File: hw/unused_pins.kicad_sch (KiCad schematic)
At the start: 0 parts

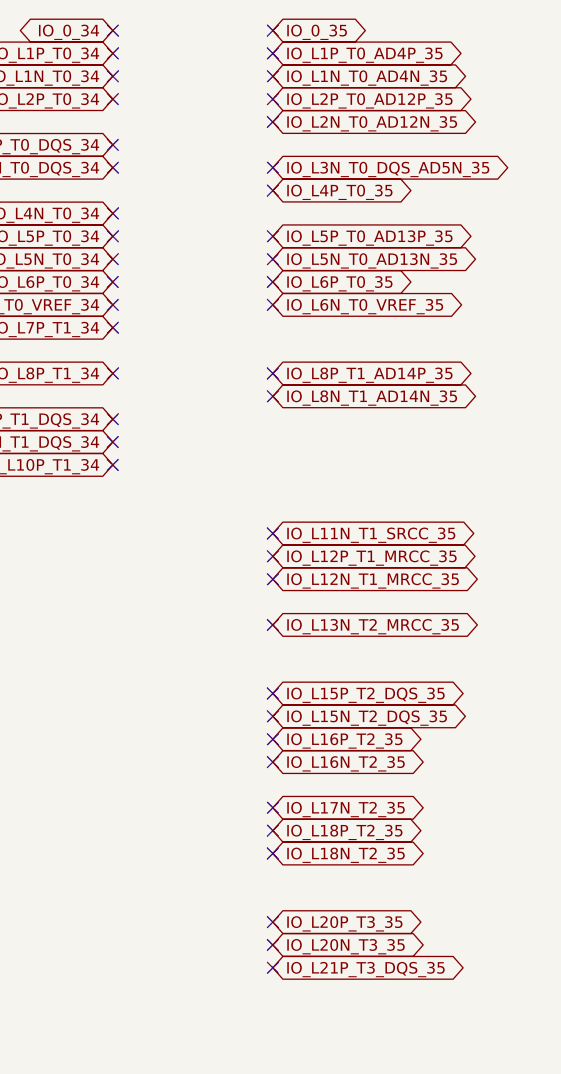
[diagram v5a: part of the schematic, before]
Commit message: finished routing; DRC passes (except for 1 hole violation at push-button)
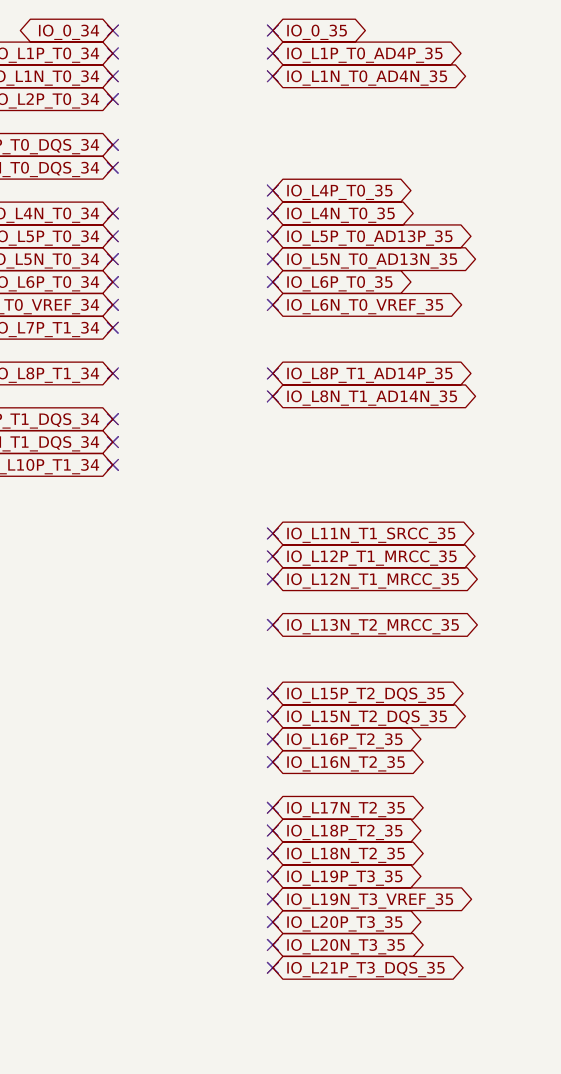
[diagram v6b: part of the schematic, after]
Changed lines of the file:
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@@
   (no_connect (at 69.85 106.68))
   (no_connect (at 69.85 149.86))
-  (no_connect (at 223.52 45.72))
   (no_connect (at 223.52 134.62))
   (no_connect (at 223.52 91.44))
   (no_connect (at 69.85 48.26))
   (no_connect (at 57.15 38.1))
-  (no_connect (at 223.52 40.64))
   (no_connect (at 57.15 93.98))
   (no_connect (at 69.85 129.54))
@@
   (no_connect (at 223.52 106.68))
   (no_connect (at 69.85 137.16))
+  (no_connect (at 223.52 124.46))
   (no_connect (at 57.15 63.5))
   (no_connect (at 223.52 33.02))
@@
   (no_connect (at 223.52 53.34))
   (no_connect (at 57.15 149.86))
+  (no_connect (at 223.52 127))
   (no_connect (at 223.52 48.26))
   (no_connect (at 205.74 38.1))
@@
   (no_connect (at 69.85 83.82))
   (no_connect (at 223.52 68.58))
-  (no_connect (at 223.52 38.1))
+  (no_connect (at 223.52 50.8))
   (no_connect (at 69.85 144.78))
   (no_connect (at 57.15 154.94))
@@
     )
   )
-  (global_label "IO_L2N_T0_AD12N_35" (shape bidirectional) (at 223.52 40.64 0) (fields_autoplaced)
-    (effects (font (size 1.27 1.27)) (justify left))
-    (property "Intersheetrefs" "${INTERSHEET_REFS}" (at 239.7264 40.64 0)
-      (effects (font (size 1.27 1.27)) (justify left) hide)
-    )
-  )
   (global_label "IO_L13N_T2_MRCC_15" (shape bidirectional) (at 57.15 96.52 180) (fields_autoplaced)
     (effects (font (size 1.27 1.27)) (justify right))
@@
     )
   )
+  (global_label "IO_L19P_T3_35" (shape bidirectional) (at 223.52 124.46 0) (fields_autoplaced)
+    (effects (font (size 1.27 1.27)) (justify left))
+    (property "Intersheetrefs" "${INTERSHEET_REFS}" (at 240.8754 124.46 0)
+      (effects (font (size 1.27 1.27)) (justify left) hide)
+    )
+  )
   (global_label "IO_L21P_T3_DQS_14" (shape bidirectional) (at 69.85 134.62 0) (fields_autoplaced)
     (effects (font (size 1.27 1.27)) (justify left))
@@
     )
   )
+  (global_label "IO_L4N_T0_35" (shape bidirectional) (at 223.52 50.8 0) (fields_autoplaced)
+    (effects (font (size 1.27 1.27)) (justify left))
+    (property "Intersheetrefs" "${INTERSHEET_REFS}" (at 239.7264 50.8 0)
+      (effects (font (size 1.27 1.27)) (justify left) hide)
+    )
+  )
+  (global_label "IO_L19N_T3_VREF_35" (shape bidirectional) (at 223.52 127 0) (fields_autoplaced)
+    (effects (font (size 1.27 1.27)) (justify left))
+    (property "Intersheetrefs" "${INTERSHEET_REFS}" (at 246.4997 127 0)
+      (effects (font (size 1.27 1.27)) (justify left) hide)
+    )
+  )
   (global_label "IO_L3P_T0_DQS_AD1P_15" (shape bidirectional) (at 57.15 43.18 180) (fields_autoplaced)
     (effects (font (size 1.27 1.27)) (justify right))
@@
     )
   )
-  (global_label "IO_L3N_T0_DQS_AD5N_35" (shape bidirectional) (at 223.52 45.72 0) (fields_autoplaced)
-    (effects (font (size 1.27 1.27)) (justify left))
-    (property "Intersheetrefs" "${INTERSHEET_REFS}" (at 244.504 45.72 0)
-      (effects (font (size 1.27 1.27)) (justify left) hide)
-    )
-  )
   (global_label "IO_L24N_T3_A00_D16_14" (shape bidirectional) (at 69.85 152.4 0) (fields_autoplaced)
     (effects (font (size 1.27 1.27)) (justify left))
@@
       (effects (font (size 1.27 1.27)) (justify left) hide)
     )
-  )
-  (global_label "IO_L2P_T0_AD12P_35" (shape bidirectional) (at 223.52 38.1 0) (fields_autoplaced)
-    (effects (font (size 1.27 1.27)) (justify left))
-    (property "Intersheetrefs" "${INTERSHEET_REFS}" (at 239.6659 38.1 0)
-      (effects (font (size 1.27 1.27)) (justify left) hide)
-    )

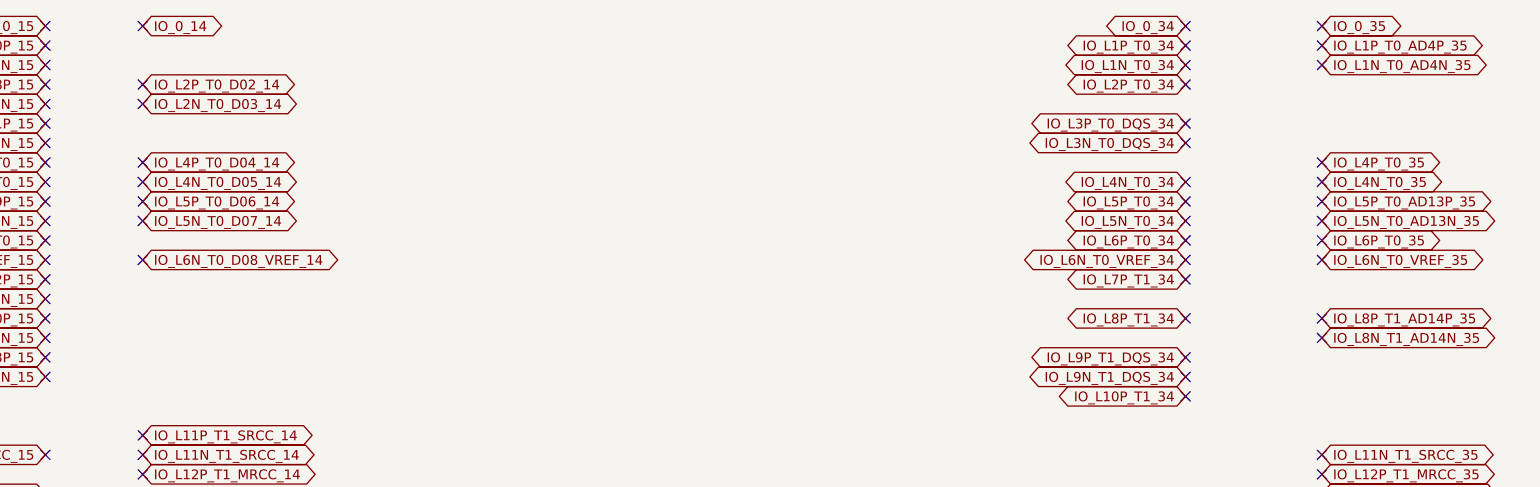
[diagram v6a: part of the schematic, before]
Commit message: added 2nd front led; more keepouts around signal lines
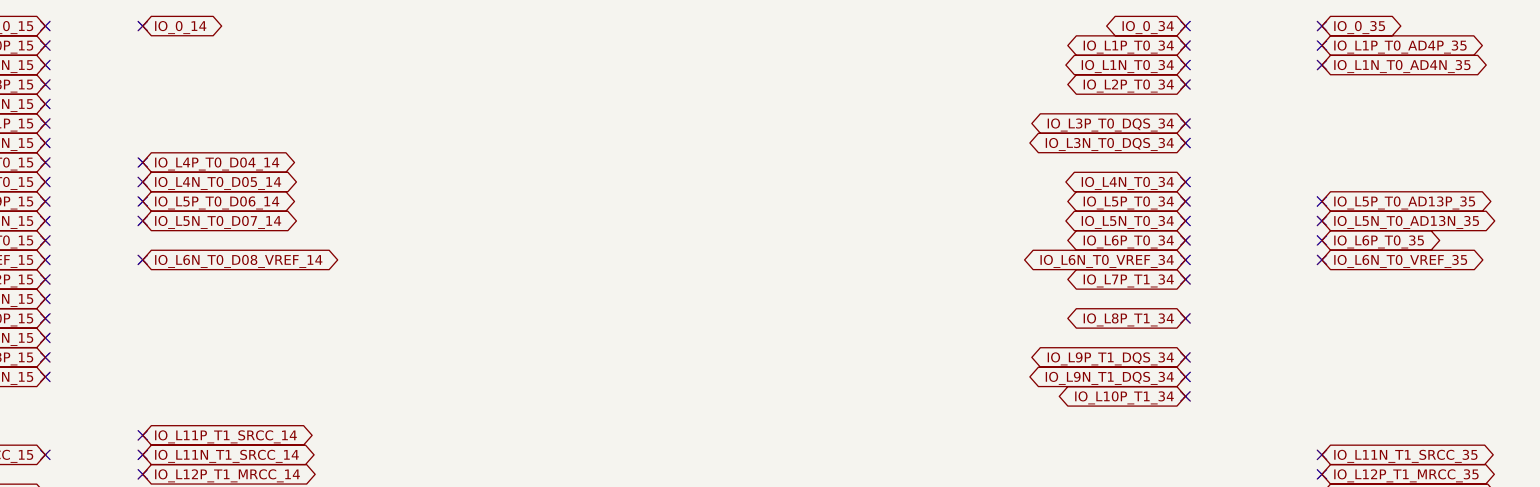
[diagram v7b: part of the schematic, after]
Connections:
- no-connect marks 117 -> 111
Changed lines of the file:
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@@
   (no_connect (at 57.15 45.72))
   (no_connect (at 57.15 71.12))
-  (no_connect (at 223.52 71.12))
   (no_connect (at 223.52 106.68))
   (no_connect (at 69.85 137.16))
@@
   (no_connect (at 57.15 63.5))
   (no_connect (at 223.52 33.02))
-  (no_connect (at 69.85 40.64))
   (no_connect (at 205.74 45.72))
   (no_connect (at 57.15 76.2))
@@
   (no_connect (at 57.15 149.86))
   (no_connect (at 223.52 127))
-  (no_connect (at 223.52 48.26))
   (no_connect (at 205.74 38.1))
   (no_connect (at 69.85 132.08))
   (no_connect (at 69.85 83.82))
-  (no_connect (at 223.52 68.58))
-  (no_connect (at 223.52 50.8))
   (no_connect (at 69.85 144.78))
   (no_connect (at 57.15 154.94))
@@
   (no_connect (at 223.52 86.36))
   (no_connect (at 57.15 68.58))
-  (no_connect (at 69.85 38.1))
   (no_connect (at 69.85 127))
   (no_connect (at 57.15 60.96))
@@
     )
   )
-  (global_label "IO_L2N_T0_D03_14" (shape bidirectional) (at 69.85 40.64 0) (fields_autoplaced)
-    (effects (font (size 1.27 1.27)) (justify left))
-    (property "Intersheetrefs" "${INTERSHEET_REFS}" (at 90.713 40.64 0)
-      (effects (font (size 1.27 1.27)) (justify left) hide)
-    )
-  )
-  (global_label "IO_L8P_T1_AD14P_35" (shape bidirectional) (at 223.52 68.58 0) (fields_autoplaced)
-    (effects (font (size 1.27 1.27)) (justify left))
-    (property "Intersheetrefs" "${INTERSHEET_REFS}" (at 239.6659 68.58 0)
-      (effects (font (size 1.27 1.27)) (justify left) hide)
-    )
-  )
   (global_label "IO_L17P_T2_A14_D30_14" (shape bidirectional) (at 69.85 114.3 0) (fields_autoplaced)
     (effects (font (size 1.27 1.27)) (justify left))
@@
     )
   )
-  (global_label "IO_L4N_T0_35" (shape bidirectional) (at 223.52 50.8 0) (fields_autoplaced)
-    (effects (font (size 1.27 1.27)) (justify left))
-    (property "Intersheetrefs" "${INTERSHEET_REFS}" (at 239.7264 50.8 0)
-      (effects (font (size 1.27 1.27)) (justify left) hide)
-    )
-  )
   (global_label "IO_L19N_T3_VREF_35" (shape bidirectional) (at 223.52 127 0) (fields_autoplaced)
     (effects (font (size 1.27 1.27)) (justify left))
@@
     )
   )
-  (global_label "IO_L2P_T0_D02_14" (shape bidirectional) (at 69.85 38.1 0) (fields_autoplaced)
-    (effects (font (size 1.27 1.27)) (justify left))
-    (property "Intersheetrefs" "${INTERSHEET_REFS}" (at 90.6525 38.1 0)
-      (effects (font (size 1.27 1.27)) (justify left) hide)
-    )
-  )
   (global_label "IO_L20N_T3_A07_D23_14" (shape bidirectional) (at 69.85 132.08 0) (fields_autoplaced)
     (effects (font (size 1.27 1.27)) (justify left))
@@
     )
   )
-  (global_label "IO_L4P_T0_35" (shape bidirectional) (at 223.52 48.26 0) (fields_autoplaced)
-    (effects (font (size 1.27 1.27)) (justify left))
-    (property "Intersheetrefs" "${INTERSHEET_REFS}" (at 239.6659 48.26 0)
-      (effects (font (size 1.27 1.27)) (justify left) hide)
-    )
-  )
   (global_label "IO_L7N_T1_AD2N_15" (shape bidirectional) (at 57.15 66.04 180) (fields_autoplaced)
     (effects (font (size 1.27 1.27)) (justify right))
@@
       (effects (font (size 1.27 1.27)) (justify left) hide)
     )
-  )
-  (global_label "IO_L8N_T1_AD14N_35" (shape bidirectional) (at 223.52 71.12 0) (fields_autoplaced)
-    (effects (font (size 1.27 1.27)) (justify left))
-    (property "Intersheetrefs" "${INTERSHEET_REFS}" (at 239.7264 71.12 0)
-      (effects (font (size 1.27 1.27)) (justify left) hide)
-    )
